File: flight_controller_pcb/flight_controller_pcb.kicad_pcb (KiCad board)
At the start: 4 copper layers, 27 x 32 mm, 69 parts, among them J1 Conn_01x08, J2 Conn_01x05, J3 Conn_01x02, U1 NRF24L01P-R7, U10 SN74LVC2T45YZP, U11 SN74LVC1T45DRL, U2 TPS62162, U3 STM32F411CEUx, U4 RFX2401C, U5 BMP390, U6 TLV70018DCKR, U7 2450LP14A0100001T, U8 ICM-20948, U9 SN74LVC2T45YZP, Y1 Crystal_GND24

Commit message: alot of work on pcb layout
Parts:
- removed the C25 at (100.7, 112.2)
- removed the C26 at (103.4, 119.5)
- removed the C27 at (103.4, 118.4)
- added C12: 0.1uF, Capacitor_SMD:C_0402_1005Metric, F.Cu at (111.6, 121.1)
- added C16: 4.7uF, Capacitor_SMD:C_0603_1608Metric, F.Cu at (115.7, 110.8)
- added C17: 0.1uF, Capacitor_SMD:C_0402_1005Metric, F.Cu at (118.5, 117.9)
- added C19: 0.1uF, Capacitor_SMD:C_0402_1005Metric, F.Cu at (116.8, 109.9)
- added C32: 0.1uF, Capacitor_SMD:C_0402_1005Metric, F.Cu at (105.8, 117.7)
- added C33: 0.1uF, Capacitor_SMD:C_0402_1005Metric, F.Cu at (107.8, 125.7)
- added C34: 0.1uF, Capacitor_SMD:C_0402_1005Metric, F.Cu at (100.7, 116.1)
- added C35: 0.1uF, Capacitor_SMD:C_0402_1005Metric, F.Cu at (101.8, 115.7)
- added C36: 0.1uF, Capacitor_SMD:C_0402_1005Metric, F.Cu at (104.1, 117.3)
- added FB1: FerriteBead, Inductor_SMD:L_0603_1608Metric, F.Cu at (107.6, 110.5)
- U10: value SN74LVC2T45YZP -> SN74LVC1T45DRL; footprint Package_BGA:Texas_DSBGA-8_0.9x1.9mm_Layout2x4_P0.5mm -> Package_TO_SOT_SMD:SOT-563
- U11: value SN74LVC1T45DRL -> ICM-20948; footprint Package_TO_SOT_SMD:SOT-563 -> Sensor_Motion:InvenSense_QFN-24_3x3mm_P0.4mm
- U8: value ICM-20948 -> SN74LVC2T45YZP; footprint ICM_20948:QFN40P300X300X105-24N -> Package_BGA:Texas_DSBGA-8_0.9x1.9mm_Layout2x4_P0.5mm
- moved C4 79.9 mm to (98.2, 137.3), turned to 180 degrees
- moved C13 79.5 mm to (93.3, 142.6), turned to 180 degrees
- moved C15 79.0 mm to (97.3, 142.1), turned to 90 degrees
- moved L2 78.0 mm to (95.1, 141.5), turned to 180 degrees
- moved L3 77.2 mm to (96.3, 141.9), turned to -90 degrees
- moved C2 77.0 mm to (91.1, 136.6), turned to 180 degrees
- moved C3 76.3 mm to (91.1, 137.7), turned to 180 degrees
- moved L4 75.7 mm to (95.1, 142.5)
- moved C6 75.2 mm to (109.1, 112.7), turned to 45 degrees
- moved C5 74.8 mm to (108.2, 111.9), turned to 45 degrees
- moved R1 73.8 mm to (98.2, 139.7)
- moved C10 73.8 mm to (93.3, 141.5), turned to 180 degrees
- moved R6 70.8 mm to (117.7, 112.8), turned to -45 degrees
- moved R7 62.7 mm to (110.7, 110.5), turned to 135 degrees
- moved R8 62.7 mm to (109.8, 111.2), turned to -45 degrees
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- renumbered C12 to C13, C13 to C14, C14 to C15, C15 to C18, C22 to C20, C23 to C21, C16 to C22, C17 to C23, C18 to C24, C19 to C25, C20 to C26, C24 to C27, D4 to D3, D3 to D4, R9 to R10, R10 to R2, R11 to R3, R2 to R4, R3 to R5, R5 to R6, R6 to R7, R7 to R8, R8 to R9, U6 to U4, U4 to U5, U5 to U6
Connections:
- C29 pad 2: +1V8 -> +3.3V
- C5 pad 1: +3.3V -> /MCU_VDDA
- C6 pad 1: +3.3V -> /MCU_VDDA
- U1 pad 3: /SPI1_SCK -> /SPI2_SCK
- U1 pad 4: /SPI1_MOSI -> /SPI2_MOSI
- U1 pad 5: /SPI1_MISO -> /SPI2_MISO
- U11 pad 1: +3.3V -> unconnected-(U11-NC-Pad1)
- U11 pad 2: GND -> unconnected-(U11-NC-Pad2)
- U11 pad 3: /ICM_CS_3V3 -> unconnected-(U11-NC-Pad3)
- U11 pad 4: /ICM_CS_1V8 -> unconnected-(U11-NC-Pad4)
- U11 pad 5: GND -> unconnected-(U11-NC-Pad5)
- U11 pad 6: +1V8 -> unconnected-(U11-NC-Pad6)
- U3 pad 11: unconnected-(U3-PA1-Pad11) -> /BMP390_IRQ
- U3 pad 12: unconnected-(U3-PA2-Pad12) -> /BMP390_CS
- U3 pad 21: unconnected-(U3-PB10-Pad21) -> /ICM_CS_3V3
- U3 pad 26: /NRF24_CSN -> /SPI2_SCK
- U3 pad 27: /BMP390_CS -> /SPI2_MISO
- U3 pad 28: /ICM_CS_3V3 -> /SPI2_MOSI
- U3 pad 29: /ESC4 -> /NRF24_CSN
- U3 pad 30: /ESC3 -> /ESC4
- U3 pad 31: /ESC2 -> /ESC3
- U3 pad 32: /ESC1 -> /ESC2
- U3 pad 33: unconnected-(U3-PA12-Pad33) -> /ESC1
- U3 pad 42: /BMP390_IRQ -> unconnected-(U3-PB6-Pad42)
- U3 pad 9: +3.3V -> /MCU_VDDA
- U9 pad B1: /SPI1_SCK -> /SPI1_MISO
- U9 pad B2: /ICM_SCK -> /ICM_MISO
- U9 pad C1: /SPI1_MOSI -> /ICM_INT_3V3
- U9 pad C2: /ICM_MOSI -> /ICM_INT_1V8
- U9 pad D2: +3.3V -> GND
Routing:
- net GND: track 0.00 -> 33.3 mm, vias 0 -> 31
- net /SPI1_MISO: track 0.38 -> 14.7 mm, vias 0 -> 3
- net /ICM_INT_3V3: track 0.00 -> 12.4 mm, vias 0 -> 2
- net /SPI1_MOSI: track 3.84 -> 14.7 mm, vias 1 -> 3
- net /SPI1_SCK: track 3.32 -> 14.1 mm, vias 2 -> 0
- net /BMP390_IRQ: track 0.00 -> 10.1 mm
- net +3.3V: track 23.0 -> 31.6 mm, vias 0 -> 5
- net /BMP390_CS: track 0.00 -> 8.62 mm
- net /V_Monitor: track 0.00 -> 8.00 mm, vias 0 -> 2
- net /BAT+: track 14.9 -> 22.5 mm, vias 0 -> 5
- net /NRF24_XC2: track 0.00 -> 7.30 mm
- net /ESC4: track 0.60 -> 7.89 mm
- net /ESC1: track 0.60 -> 7.21 mm
- net /ESC2: track 0.60 -> 7.16 mm
- net /ESC3: track 0.85 -> 7.22 mm
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- added copper zone on In2.Cu, net +3.3V

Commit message: routing work
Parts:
- moved C8 87.9 mm to (116.9, 129.1)
- moved R1 29.5 mm to (121.6, 121.6), turned to -45 degrees
- moved C4 28.5 mm to (120.2, 119.2), turned to 135 degrees
- moved U1 28.3 mm to (118.0, 121.8), turned to -45 degrees
- moved C3 27.8 mm to (115.0, 123.4), turned to -135 degrees
- moved C2 27.0 mm to (114.1, 122.6), turned to -135 degrees
- moved Y1 26.9 mm to (112.4, 128.1), turned to 180 degrees
- moved C21 7.20 mm to (108.0, 105.1), turned to 0 degrees
- moved U10 6.47 mm to (109.8, 117.3)
- moved C30 6.47 mm to (110.4, 119.4)
- moved C33 6.47 mm to (109.2, 119.4)
- moved U4 6.41 mm to (107.8, 102.6), turned to -90 degrees
- moved FB1 5.64 mm to (111.8, 106.6)
- moved C20 4.51 mm to (109.8, 102.6), turned to 90 degrees
- moved C5 4.41 mm to (109.9, 107.8), turned to 135 degrees
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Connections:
- U3 pad 19: /NRF_IRQ -> unconnected-(U3-PB1-Pad19)
- U3 pad 25: /NRF24_CE -> /NRF_IRQ
- U3 pad 30: /ESC4 -> /NRF24_CE
- U3 pad 31: /ESC3 -> /ESC4
- U3 pad 32: /ESC2 -> /ESC3
- U3 pad 33: /ESC1 -> /ESC2
- U3 pad 34: unconnected-(U3-PA13-Pad34) -> /ESC1
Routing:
- net +3.3V: track 31.6 -> 92.3 mm, vias 5 -> 11
- net GND: track 33.3 -> 52.0 mm, vias 31 -> 43
- net /ICM_INT_3V3: track 12.4 -> 0.78 mm, vias 2 -> 1
- net /NRF24_XC1: track 3.55 -> 12.5 mm
- net /BAT+: track 22.5 -> 29.4 mm, vias 5 -> 2
- net Net-(D1-K): track 1.87 -> 8.64 mm
- net /ICM_CS_1V8: track 5.85 -> 11.9 mm
- net /NRF_IRQ: track 0.00 -> 4.48 mm
- net /NRF24_XC2: track 7.30 -> 11.7 mm
- net /SPI2_MOSI: track 0.00 -> 4.20 mm
- net /SPI2_MISO: track 0.00 -> 4.14 mm
- net /NRF24_CSN: track 0.00 -> 4.01 mm
- net /NRF24_CE: track 0.00 -> 3.70 mm
- net /SPI2_SCK: track 0.88 -> 4.15 mm, vias 1 -> 2
- net /ICM_CS_3V3: track 5.06 -> 1.99 mm
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
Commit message: more routing
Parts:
- moved C11 88.4 mm to (116.8, 125.8), turned to -135 degrees
- moved C13 30.4 mm to (119.0, 126.2)
- moved L4 30.2 mm to (119.2, 124.2), turned to -135 degrees
- moved L2 30.2 mm to (119.1, 123.2), turned to -135 degrees
- moved U5 12.9 mm to (114.2, 135.9)
- moved C8 6.63 mm to (111.9, 124.7), turned to 135 degrees
- moved Y1 4.51 mm to (114.6, 124.2), turned to -45 degrees
- moved C3 2.35 mm to (113.2, 121.8)
- moved C2 2.35 mm to (112.3, 121.0)
- moved C4 2.01 mm to (118.5, 118.0), turned to -45 degrees
- moved U1 1.22 mm to (117.1, 120.9)
- moved R1 1.22 mm to (120.8, 120.7)
- moved U11 0.50 mm to (102.5, 119.2)
- moved C29 0.47 mm to (106.3, 114.4), turned to 180 degrees
- moved C36 0.40 mm to (104.1, 116.5)
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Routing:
- net +3.3V: track 92.3 -> 121.7 mm, vias 11 -> 16
- net /NRF24_XC1: track 12.5 -> 7.30 mm
- net GND: track 52.0 -> 54.3 mm, vias 43 -> 48
- net /NRF24_ANT1: track 2.80 -> 4.91 mm
- net +1V8: track 9.71 -> 11.6 mm, vias 0 -> 2
- net Net-(U1-DVDD): track 4.09 -> 2.67 mm, vias 1 -> 0
- net /SPI2_MOSI: track 4.20 -> 5.52 mm
- net /NRF24_ANT2: track 2.81 -> 4.13 mm
- net /SPI2_MISO: track 4.14 -> 5.32 mm
- net /ESC1: track 5.82 -> 6.60 mm
- net /NRF24_XC2: track 11.7 -> 12.5 mm
- net /ESC4: track 7.38 -> 8.12 mm
- net /ESC3: track 6.75 -> 7.50 mm
- net /ESC2: track 6.30 -> 7.04 mm
- net /NRF24_CE: track 3.70 -> 4.41 mm
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
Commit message: more routing
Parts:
- moved C25 88.0 mm to (116.2, 130.6), turned to -90 degrees
- moved C23 87.0 mm to (119.0, 130.6), turned to -90 degrees
- moved C18 84.9 mm to (115.8, 128.3), turned to 90 degrees
- moved C24 71.5 mm to (117.6, 129.3), turned to 90 degrees
- moved R10 69.9 mm to (112.3, 125.2), turned to 180 degrees
- moved U7 62.4 mm to (108.5, 129.5)
- moved C10 27.6 mm to (114.9, 124.2)
- moved L3 27.1 mm to (117.2, 124.7)
- moved C15 25.3 mm to (117.2, 126.5), turned to -90 degrees
- moved C2 9.04 mm to (121.4, 121.5), turned to 0 degrees
- moved C3 8.31 mm to (121.4, 120.4), turned to 0 degrees
- moved U5 7.52 mm to (112.9, 128.5), turned to 180 degrees
- moved C13 4.22 mm to (114.9, 125.2)
- moved C11 4.19 mm to (112.9, 124.2), turned to 180 degrees
- moved C8 3.45 mm to (110.5, 121.6), turned to -90 degrees
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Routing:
- net GND: track 54.3 -> 78.4 mm, vias 48 -> 69
- net /NRF24_CE: track 4.41 -> 17.4 mm, vias 0 -> 2
- net +3.3V: track 121.7 -> 128.2 mm
- net /NRF24_VDD_PA: track 4.58 -> 8.68 mm
- net Net-(U5-TXRX): track 0.00 -> 3.20 mm
- net Net-(U5-RXEN): track 0.00 -> 1.98 mm
- net /SPI2_MISO: track 5.32 -> 3.68 mm
- net /SPI2_MOSI: track 5.52 -> 4.03 mm
- net /NRF_IRQ: track 5.02 -> 3.61 mm
- net Net-(C15-Pad1): track 1.15 -> 2.13 mm
- net /NRF24_XC2: track 12.5 -> 13.0 mm

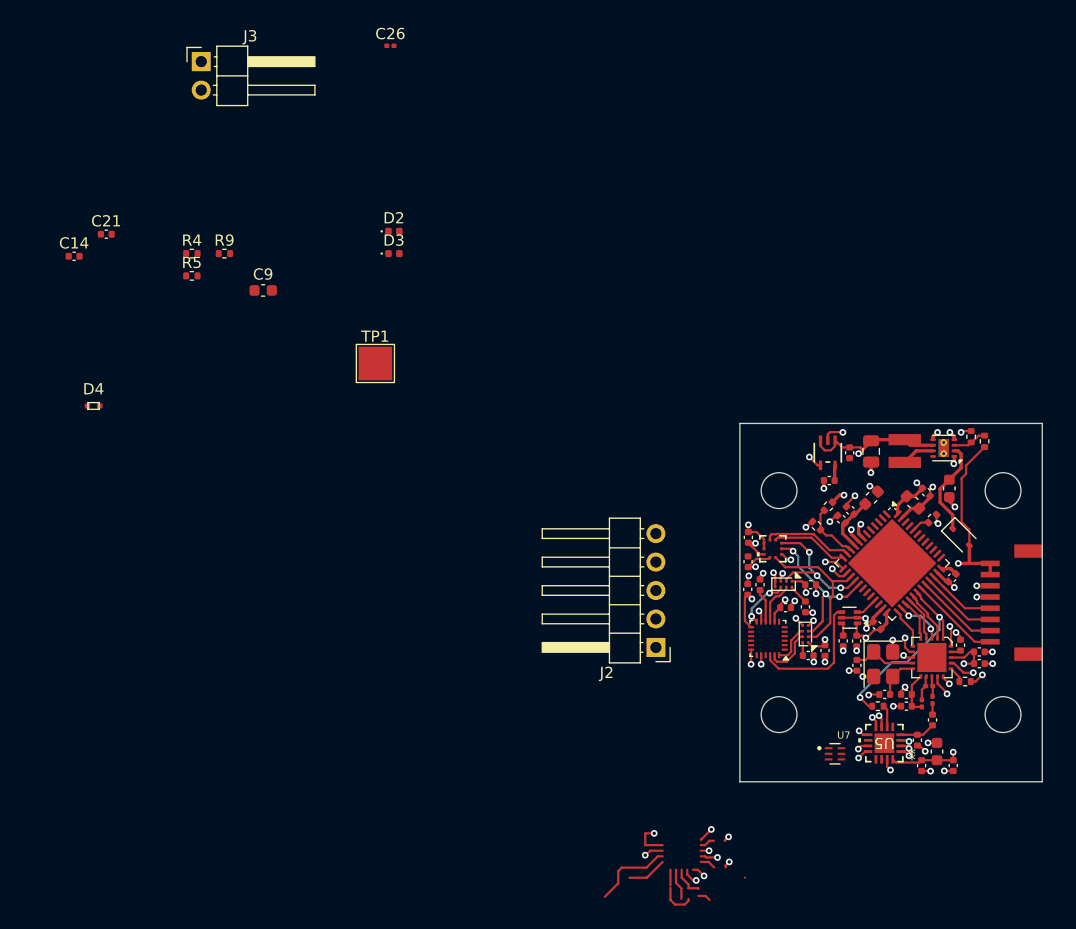
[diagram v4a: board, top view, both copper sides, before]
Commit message: finished most of the traces
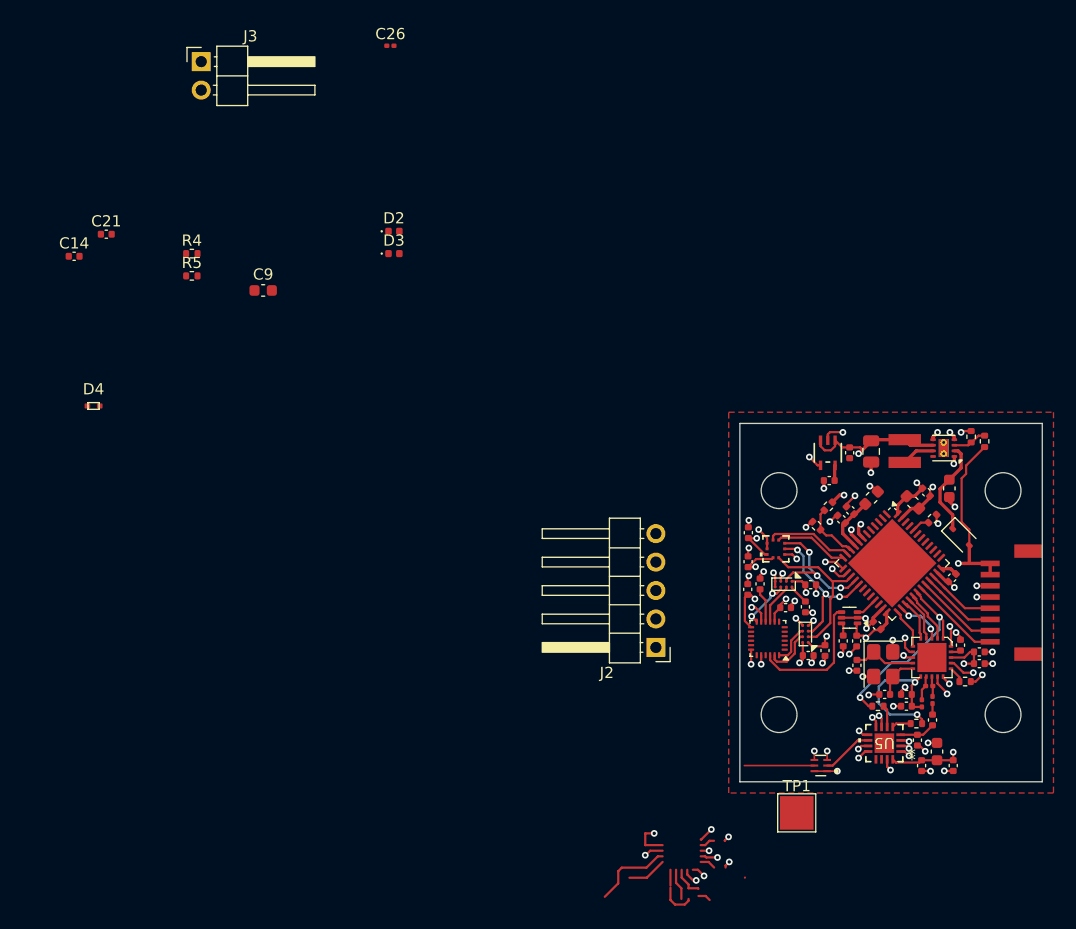
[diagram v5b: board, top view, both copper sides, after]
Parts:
- moved R9 74.7 mm to (115.8, 126.8)
- moved TP1 55.0 mm to (105.1, 134.8)
- moved U7 1.65 mm to (107.2, 130.6), turned to 180 degrees
- moved C27 0.42 mm to (100.8, 109.8)
- moved U6 0.28 mm to (103.2, 111.2)
- moved C35 0.08 mm to (101.8, 114.3)
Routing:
- net /NRF24_VDD_PA: track 8.68 -> 18.5 mm, vias 0 -> 2
- net GND: track 78.4 -> 85.0 mm, vias 69 -> 74
- net Net-(U7-OUT): track 0.00 -> 6.25 mm
- net Net-(U5-ANT): track 0.00 -> 4.60 mm
- net Net-(U5-TXEN): track 0.00 -> 1.72 mm
- net +3.3V: track 128.2 -> 129.4 mm
- net +1V8: track 11.6 -> 12.7 mm, vias 2 -> 3
- added copper zone on F.Cu, net GND
- added copper zone on In1.Cu, net GND

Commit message: more routing
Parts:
- removed the C21 at (43.4, 83.1)
- moved R4 82.6 mm to (120.0, 130.4), turned to 90 degrees
- moved R5 82.6 mm to (121.2, 130.4), turned to 90 degrees
- moved C26 76.8 mm to (109.8, 131.2), turned to 90 degrees
- moved D2 74.8 mm to (124.0, 133.7), turned to 180 degrees
- moved J3 73.1 mm to (118.6, 97.7), turned to 90 degrees
- moved D4 72.5 mm to (114.8, 99.9)
- moved C14 72.2 mm to (108.3, 109.9), turned to -135 degrees
- moved D3 72.0 mm to (124.0, 131.4), turned to 180 degrees
- moved C9 62.6 mm to (109.8, 122.4), turned to 45 degrees
- moved J2 24.3 mm to (102.1, 97.7), turned to 90 degrees
- moved C3 8.84 mm to (112.8, 122.4), turned to 180 degrees
- moved C2 8.61 mm to (112.8, 121.3), turned to 180 degrees
- moved R1 4.55 mm to (119.2, 127.5), turned to -90 degrees
- moved C24 4.25 mm to (118.4, 133.5)
- moved C13 3.94 mm to (114.3, 129.2)
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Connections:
- J3 pad 1: GND -> Net-(D4-A)
- J3 pad 2: Net-(D4-A) -> GND
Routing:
- net +1V8: track 12.7 -> 52.6 mm, vias 3 -> 6
- net +3.3V: track 129.4 -> 160.1 mm
- net /STATUS_LED: track 0.00 -> 23.4 mm, vias 0 -> 2
- net /ERROR_LED: track 0.00 -> 20.9 mm, vias 0 -> 2
- net /SWDIO: track 1.86 -> 19.7 mm
- net /SWCLK: track 1.77 -> 19.4 mm
- net /NRST: track 1.21 -> 18.1 mm, vias 1 -> 2
- net /NRF24_XC2: track 13.0 -> 5.71 mm
- net Net-(U3-VCAP1): track 0.00 -> 6.95 mm
- net /NRF24_CE: track 17.4 -> 23.5 mm
- net /NRF24_VDD_PA: track 18.5 -> 13.1 mm
- net Net-(D2-A): track 0.00 -> 4.67 mm
- net /SPI2_MISO: track 3.68 -> 7.83 mm
- net Net-(D4-A): track 0.00 -> 4.12 mm
- net /NRF_IRQ: track 3.61 -> 7.66 mm
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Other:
- board size 27 x 32 mm -> 27 x 41.2 mm
- board text added: "Error"
- board text added: "Status"

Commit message: more routing
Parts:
- moved U11 0.60 mm to (102.5, 119.8)
- moved J1 0.50 mm to (123.8, 116.0)
- moved C36 0.45 mm to (103.8, 116.8)
- moved U10 0.23 mm to (110.0, 117.3)
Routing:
- net /ICM_INT_3V3: track 2.36 -> 10.9 mm
- net +1V8: track 52.6 -> 47.5 mm
- net GND: track 85.8 -> 87.5 mm
- net /SWDIO: track 19.7 -> 20.8 mm
- net /SWCLK: track 19.4 -> 20.3 mm
- net /ICM_INT_1V8: track 4.72 -> 5.50 mm
- net /NRF24_VDD_PA: track 13.1 -> 13.9 mm
- net /ICM_SCK: track 4.46 -> 5.10 mm
- net /ICM_MOSI: track 3.58 -> 4.18 mm
- net Net-(U11-REGOUT): track 3.10 -> 3.70 mm
- net /ICM_MISO: track 3.70 -> 4.30 mm
- net +3.3V: track 160.1 -> 160.6 mm
- net /ESC2: track 6.87 -> 6.37 mm
- net /ESC3: track 7.50 -> 7.00 mm
- net /ESC1: track 6.35 -> 5.85 mm
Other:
- board size 27 x 41.2 mm -> 27.2 x 41.2 mm
